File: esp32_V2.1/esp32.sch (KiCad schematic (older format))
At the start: 71 parts, among them IC1 KF33BD-TR, J1 USB_C, J2 Conn_01x26, J3 Conn_01x26, J4 pH, J5 ORP, Q2 8205A, Q3 BC817, Q4 BC817, SW1 Reset, SW2 Boot, U1 CH340G, U2 TC4056, U3 DW01A, U4 LM358, U5 TLC272, U6 LM358, X1 12 MHz

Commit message: Finished routing
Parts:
- IC1: symbol KF33BDT-TR:KF33BD-TR -> esp32-rescue:KF33BD-TR-KF33BDT-TR
- J1: symbol USB_C_Receptacle_2.0:USB_C_Receptacle_2.0 -> esp32-rescue:USB_C_Receptacle_2.0-USB_C_Receptacle_2.0
- Q2: symbol 8205A:8205A -> esp32-rescue:8205A-8205A
- U3: symbol DW01A:DW01A -> esp32-rescue:DW01A-DW01A
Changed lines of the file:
@@
 EESchema Schematic File Version 4
-LIBS:esp32-cache
-EELAYER 29 0
+EELAYER 30 0
 EELAYER END
 $Descr A4 11693 8268
@@
 	3400 4250 3400 4650
 $Comp
-L DW01A:DW01A U3
+L esp32-rescue:DW01A-DW01A U3
 U 1 1 6294CD9F
 P 2050 6400
@@
 	3700 5550 6350 5550
 $Comp
-L 8205A:8205A Q2
+L esp32-rescue:8205A-8205A Q2
 U 1 1 62B9C3B7
 P 2050 7150
@@
 	5150 7100 5050 7100
 $Comp
-L USB_C_Receptacle_2.0:USB_C_Receptacle_2.0 J1
+L esp32-rescue:USB_C_Receptacle_2.0-USB_C_Receptacle_2.0 J1
 U 1 1 63686CC8
 P 1150 1850
@@
 Connection ~ 1250 4700
 $Comp
-L KF33BDT-TR:KF33BD-TR IC1
+L esp32-rescue:KF33BD-TR-KF33BDT-TR IC1
 U 1 1 63375022
 P 5000 6600

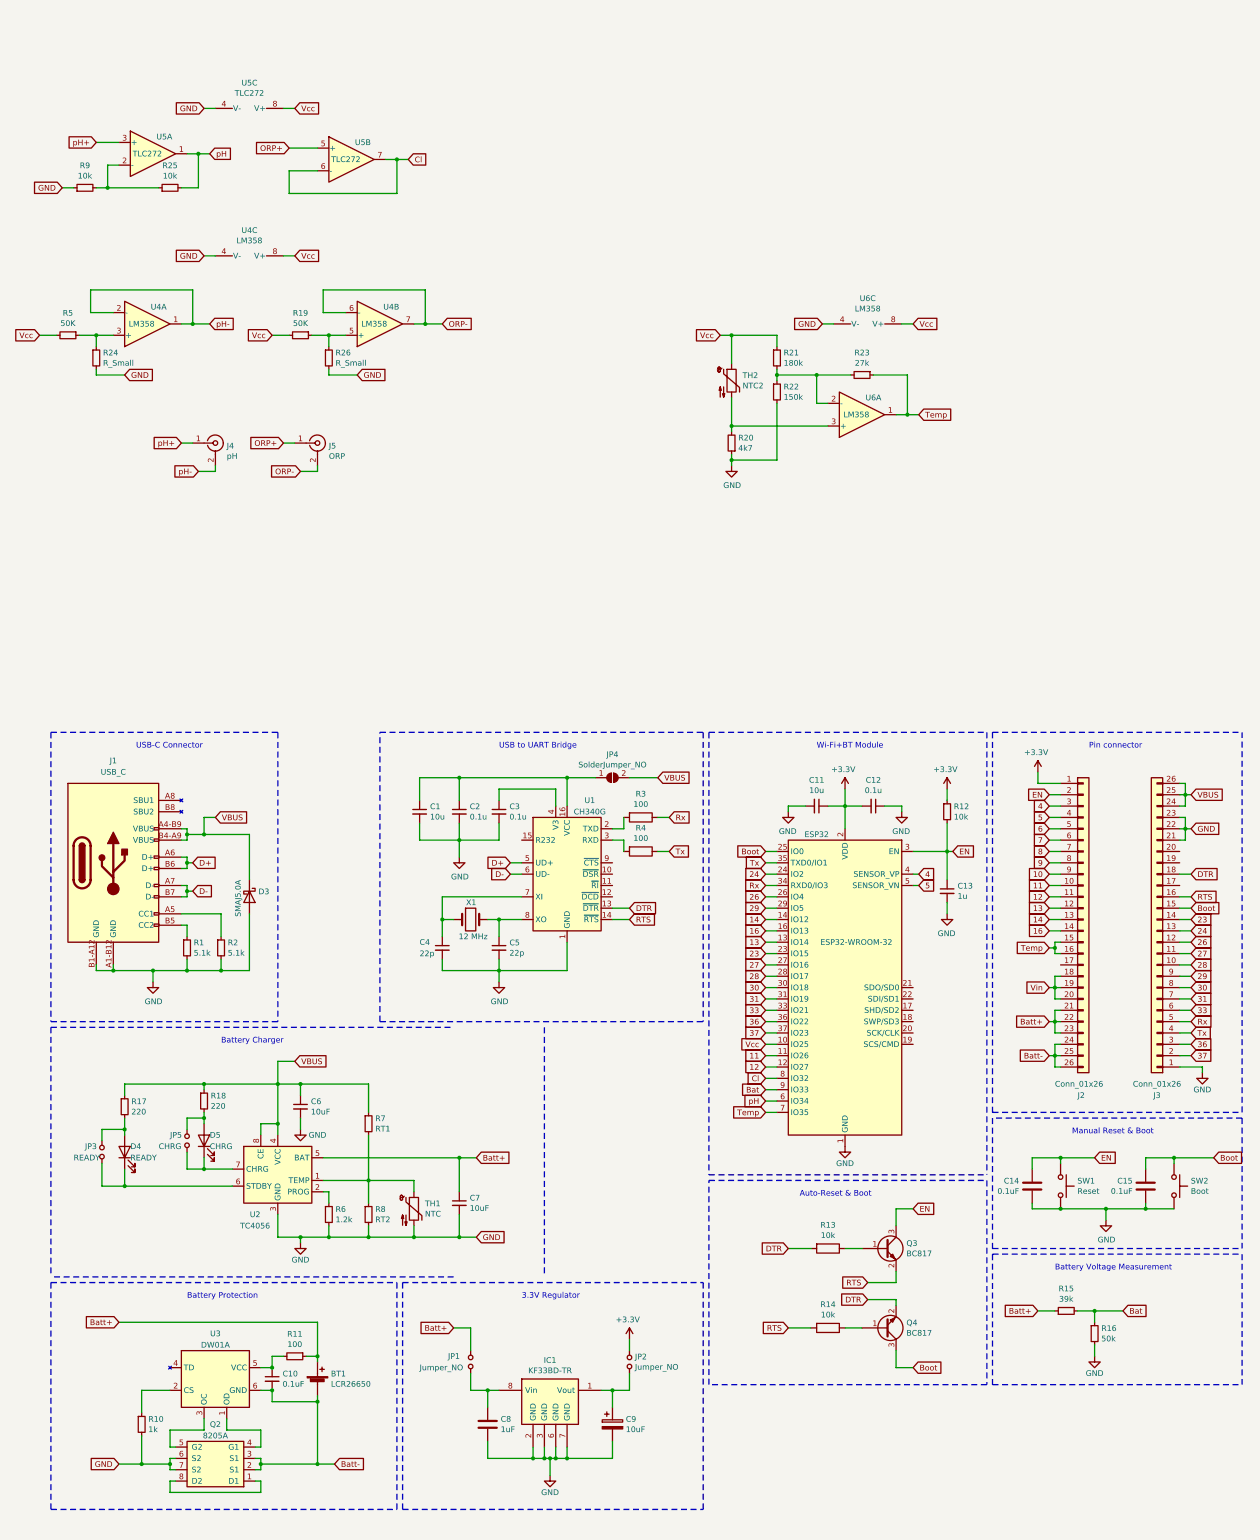
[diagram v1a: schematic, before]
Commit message: Made final changes. Added jumpers for Vcc, bat and buttons
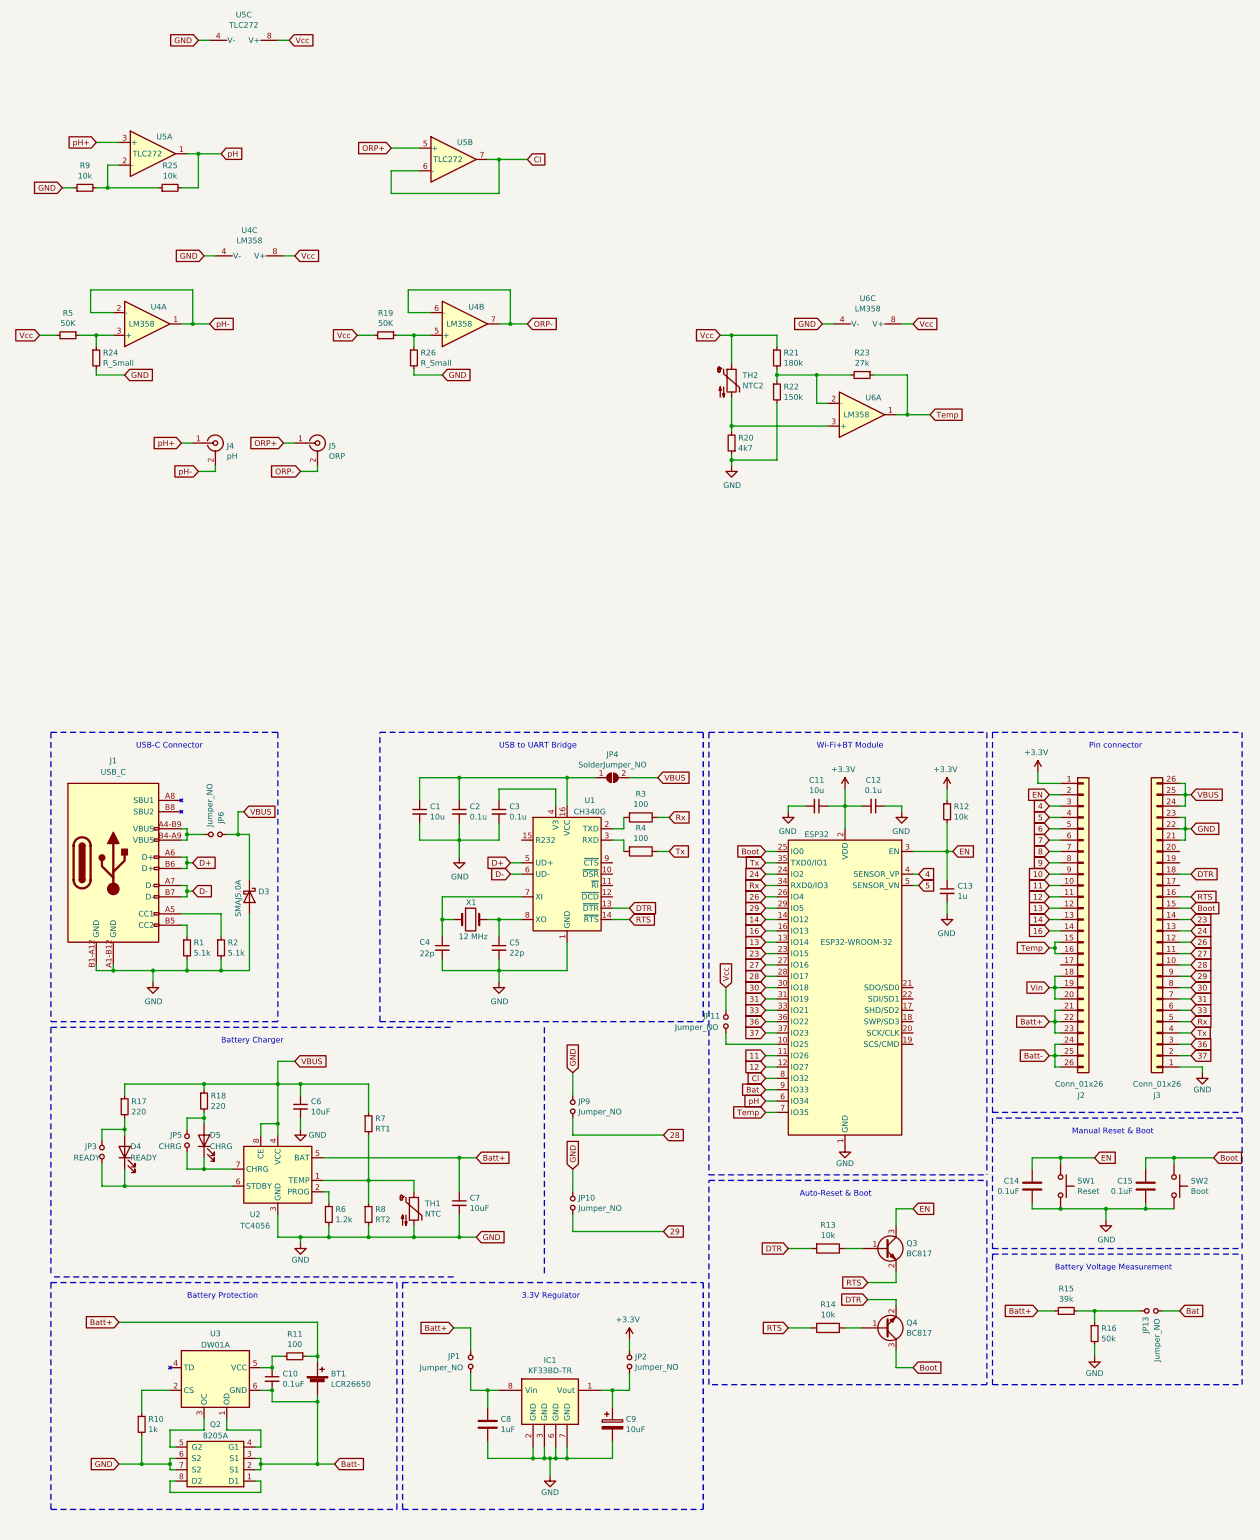
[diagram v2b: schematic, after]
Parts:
- added JP10, JP11, JP13, JP6, JP9: Jumper_NO, Connector_PinSocket_2.54mm:PinSocket_1x02_P2.54mm_Vertical, symbol Device:Jumper_NO_Small
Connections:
- net 28: now also JP9.1
- net 29: now also JP10.1
- net Bat: now also JP13.1; no longer R15.2, R16.1
- net GND: now also JP10.2, JP9.2
- net VBUS: now also JP6.2; no longer J1.A4-B9 (VBUS), J1.B4-A9 (VBUS)
- net Vcc: now also JP11.2; no longer ESP32.10 (IO25)
- new net: ESP32.10 (IO25), JP11.1
- new net: JP13.2, R15.2, R16.1
- new net: J1.A4-B9 (VBUS), J1.B4-A9 (VBUS), JP6.1
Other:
- moved on the sheet: R19, R26, U4B, U5B, U5C

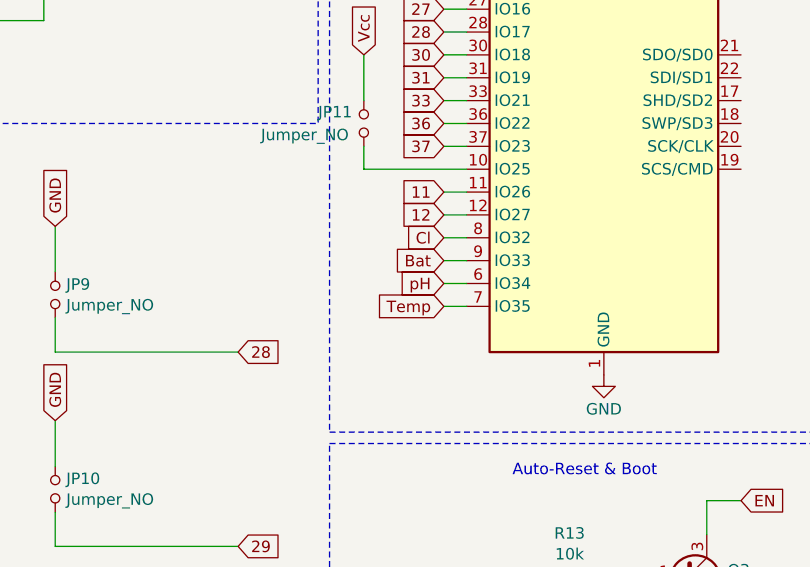
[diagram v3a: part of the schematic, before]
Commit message: Refactor some tracks
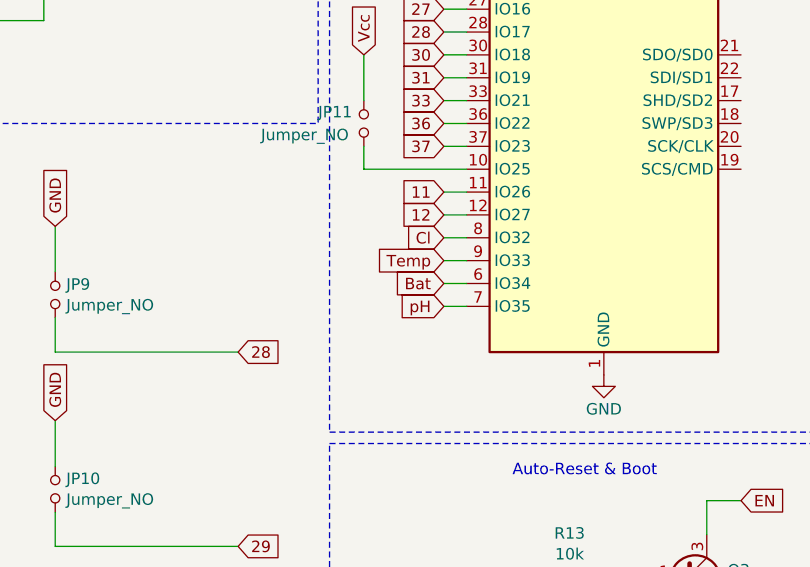
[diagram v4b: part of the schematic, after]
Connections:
- net Bat: now also ESP32.6 (IO34); no longer ESP32.9 (IO33)
- net Temp: now also ESP32.9 (IO33); no longer ESP32.7 (IO35)
- net pH: now also ESP32.7 (IO35); no longer ESP32.6 (IO34)
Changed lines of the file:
@@
 	6900 3950 7000 3950
 Text GLabel 6900 3950 0    50   Input ~ 0
-pH
+Bat
 Text GLabel 6900 3850 0    50   Input ~ 0
-Bat
+Temp
 Wire Wire Line
 	6900 2450 7000 2450
@@
 	6900 4050 7000 4050
 Text GLabel 6900 4050 0    50   Input ~ 0
-Temp
+pH
 Wire Wire Line
 	6900 2150 7000 2150
